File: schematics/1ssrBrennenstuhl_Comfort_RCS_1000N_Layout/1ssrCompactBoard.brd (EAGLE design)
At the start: 46 x 47 mm, 20 parts, among them K1 AQG12105

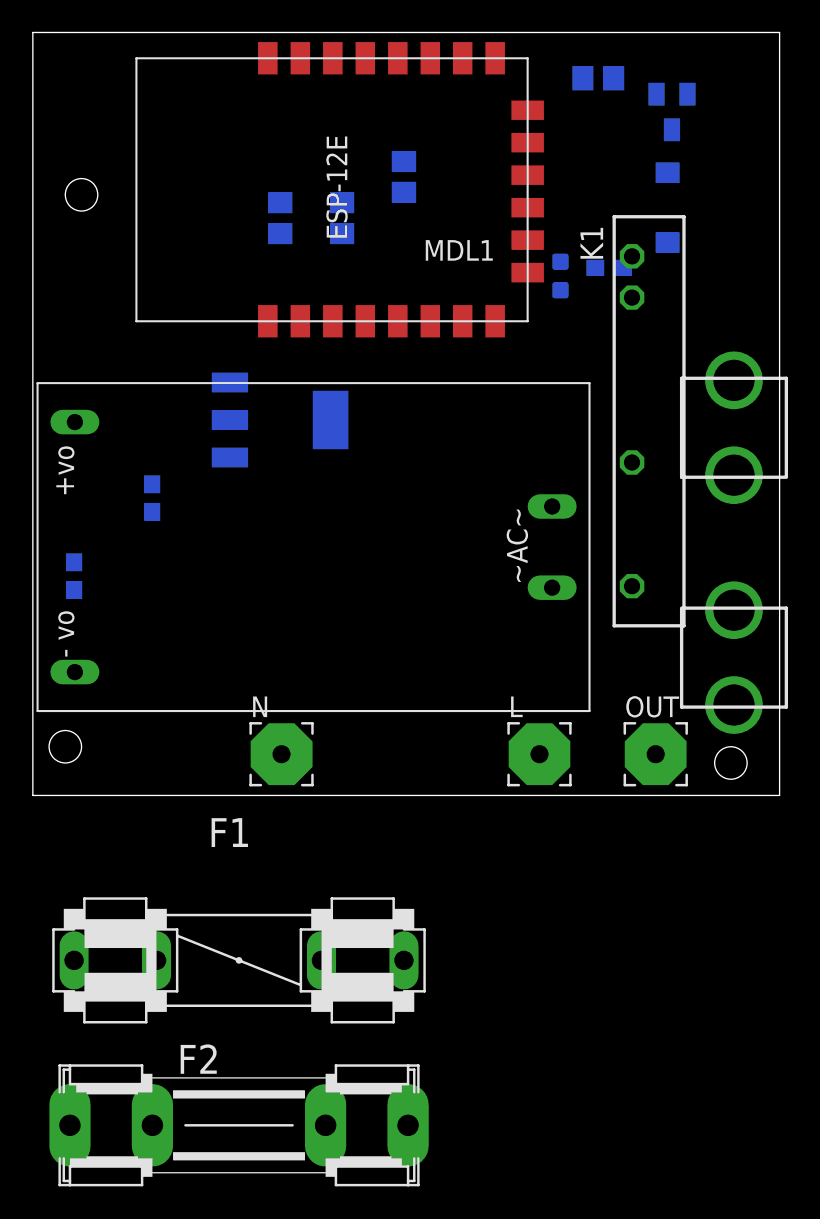
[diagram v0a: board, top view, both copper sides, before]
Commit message: placed fuse on pcb
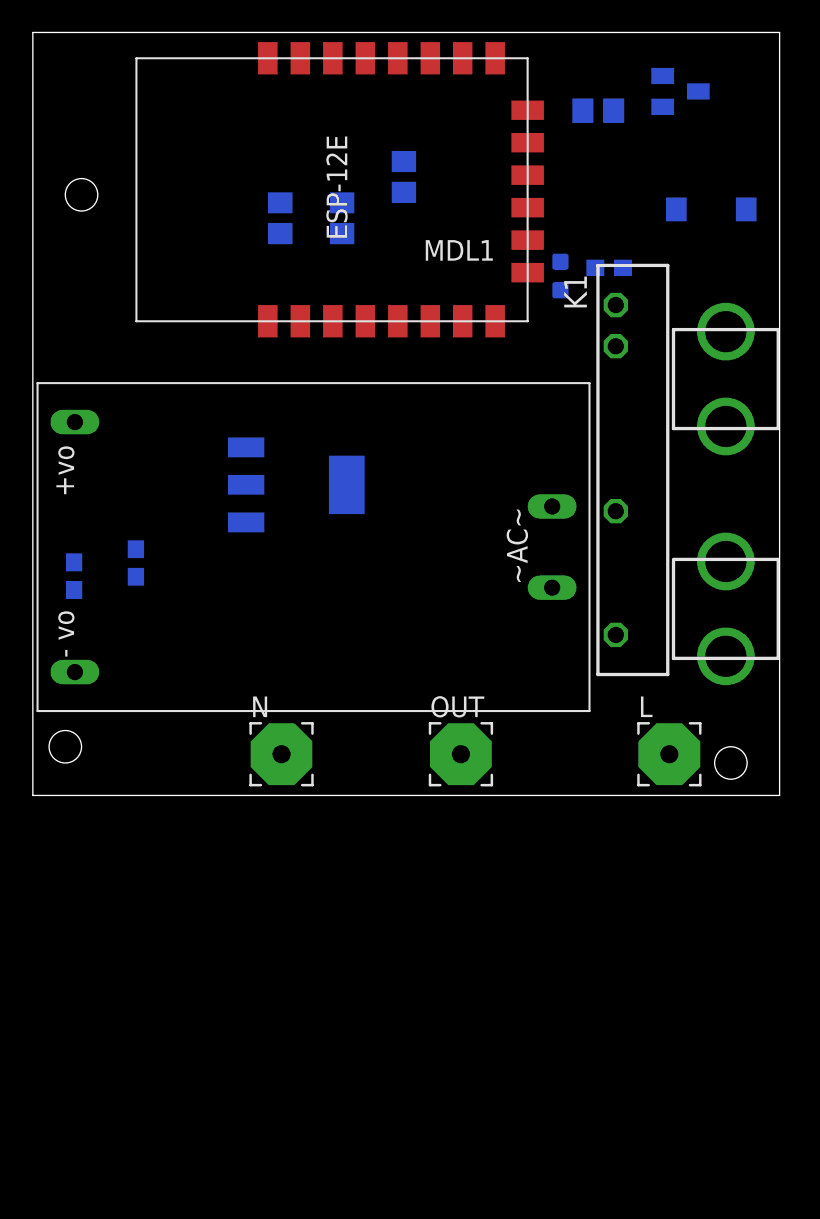
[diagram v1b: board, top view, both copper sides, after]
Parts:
- removed F1: (no value), special:FUSE1
- removed F2: (no value), fuse:SHK20L
- removed F3: FUSEX20MM, SparkFun-Passives:FUSE_5MM
- added FUSE: FUSEX20MM, SparkFun-Passives:FUSE_5MM
- moved OUT 12.0 mm to (26.4, 2.54)
- moved L 8.00 mm to (39.2, 2.54)
- moved C2 4.12 mm to (6.35, 14.3)
- moved U2 4.12 mm to (16.2, 19.1)
- moved K1 3.16 mm to (35.9, 20.1)
- moved D1 2.69 mm to (41.8, 36.1), turned to 180 degrees
- moved R3 2.00 mm to (34.8, 42.2)
- moved Q1 1.38 mm to (39.9, 43.4), turned to 90 degrees
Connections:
- net ACLOUT renamed OUT
- removed net ACLIN: K1.O1, L.1, U$4.AC1
- removed net ACN: N.1, U$4.AC2
- new net FUSED_LINE: FUSE.3, K1.O1, U$4.AC2
- new net LINE: FUSE.1, L.1
- new net NEUTRAL: N.1, U$4.AC1

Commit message: board routing work in progress
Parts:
- added J1: (no value), SparkFun-Connectors:1X02_LONGPADS
- added R6: 10K, resistor:R0805
- moved R4 5.41 mm to (32.5, 28.0), turned to 270 degrees
- moved Q1 4.81 mm to (36.6, 39.9), turned to 180 degrees
- moved D1 3.58 mm to (38.3, 35.4)
- moved R1 3.18 mm to (25.0, 35.8)
- moved OUT 2.50 mm to (28.9, 2.54)
- moved FUSE 2.00 mm to (42.7, 16.6)
- moved R5 1.90 mm to (14.5, 33.8)
- moved R2 1.83 mm to (18.5, 33.8)
- moved C1 1.75 mm to (2.54, 11.8)
- moved R3 1.42 mm to (33.4, 41.9), turned to 270 degrees
- moved C2 1.33 mm to (6.50, 13.0)
- moved MDL1 1.00 mm to (30.5, 28.2)
- moved U$4 0.50 mm to (34.3, 24.9)
- moved U2 0.27 mm to (16.0, 19.0)
- moved K1 0.25 mm to (35.9, 19.8)
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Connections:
- net 3V3: now also R6.2
- net GND: now also J1.1
- net GPIO4: now also J1.2, R6.1
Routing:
- net GND: track 0.00 -> 97.3 mm, vias 0 -> 1
- net 5V: track 0.00 -> 57.4 mm
- net 3V3: track 0.00 -> 55.8 mm, vias 0 -> 2
- net GPIO4: track 0.00 -> 28.1 mm, vias 0 -> 1
- net NEUTRAL: track 0.00 -> 19.3 mm
- net FUSED_LINE: track 0.00 -> 17.6 mm
- net GPIO5: track 0.00 -> 17.0 mm, vias 0 -> 1
- net N$10: track 0.00 -> 13.6 mm
- net LINE: track 0.00 -> 11.1 mm
- net OUT: track 0.00 -> 10.00 mm
- net GPIO0: track 0.00 -> 8.71 mm, vias 0 -> 1
- net N$9: track 0.00 -> 4.65 mm, vias 0 -> 1
- net N$6: track 0.00 -> 4.65 mm, vias 0 -> 1
- net N$1: track 0.00 -> 2.27 mm
- net N$12: track 0.00 -> 2.24 mm

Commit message: board routing work in progress
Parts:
- moved L 1.00 mm to (38.5, 2.54)
- moved U$4 0.25 mm to (34.0, 24.9)
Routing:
- net FUSED_LINE: track 17.6 -> 11.8 mm
- net LINE: track 11.1 -> 5.84 mm
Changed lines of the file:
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@@
 <element name="R3" library="resistor" package="R0805" value="10K" x="33.43" y="41.92" rot="MR270"/>
 <element name="R5" library="resistor" package="R0805" value="10K" x="14.5" y="33.81" rot="MR270"/>
-<element name="U$4" library="hlk-pm01" package="HLK-PM01" value="HLK-PM01" x="34.29" y="24.9" rot="R180"/>
+<element name="U$4" library="hlk-pm01" package="HLK-PM01" value="HLK-PM01" x="34.04" y="24.9" rot="R180"/>
 <element name="U2" library="SparkFun-PowerIC" package="SOT223" value="" x="16" y="19" rot="MR90">
 <attribute name="PROD_ID" value="VREG-08170" x="16" y="19" size="1.778" layer="28" rot="MR90" display="off"/>
@@
 <element name="R1" library="resistor" package="R0805" value="10K" x="25" y="35.75" rot="MR270"/>
 <element name="N" library="wirepad" package="3,81/1,1" value="" x="15.32" y="2.54"/>
-<element name="L" library="wirepad" package="3,81/1,1" value="" x="39.46" y="2.54"/>
+<element name="L" library="wirepad" package="3,81/1,1" value="" x="38.46" y="2.54"/>
 <element name="OUT" library="wirepad" package="3,81/1,1" value="" x="28.87" y="2.54"/>
 <element name="D2" library="SparkFun-LED" package="LED-0603" value="" x="32.5" y="32" rot="MR0"/>
@@
 <wire x1="37.5559875" y1="43.5640125" x2="34.606975" y2="46" width="0.4064" layer="16" curve="45"/>
 <wire x1="34.606975" y1="46" x2="28.5" y2="46" width="0.4064" layer="16"/>
-<wire x1="2.59" y1="7.1" x2="4.836975" y2="7.1" width="0.4064" layer="1"/>
+<wire x1="2.34" y1="7.1" x2="4.836975" y2="7.1" width="0.4064" layer="1"/>
 <wire x1="4.836975" y1="7.1" x2="5.2859875" y2="7.2859875" width="0.4064" layer="1" curve="45"/>
 <wire x1="5.2859875" y1="7.2859875" x2="6" y2="8" width="0.4064" layer="1"/>
@@
 <wire x1="6" y1="37.486975" x2="5.8140125" y2="37.9359875" width="0.4064" layer="1" curve="45"/>
 <wire x1="5.8140125" y1="37.9359875" x2="3" y2="40.75" width="0.4064" layer="1"/>
-<wire x1="2.59" y1="7.1" x2="2.59" y2="10.789290625" width="0.4064" layer="16"/>
+<wire x1="2.34" y1="7.1" x2="2.59" y2="10.789290625" width="0.4064" layer="16"/>
 <wire x1="2.59" y1="10.789290625" x2="2.54" y2="10.91" width="0.4064" layer="16" curve="45"/>
 </signal>
@@
 <contactref element="R4" pad="2"/>
 <wire x1="2.54" y1="12.61" x2="2.59" y2="12.61" width="0.4064" layer="16"/>
-<wire x1="2.59" y1="12.61" x2="2.59" y2="22.5" width="0.4064" layer="16"/>
+<wire x1="2.59" y1="12.61" x2="2.34" y2="22.5" width="0.4064" layer="16"/>
 <wire x1="32.5" y1="27.15" x2="35.376975" y2="27.15" width="0.4064" layer="16"/>
 <wire x1="35.376975" y1="27.15" x2="35.8259875" y2="27.3359875" width="0.4064" layer="16" curve="45"/>
@@
 <wire x1="38.25" y1="30.023025" x2="38.0640125" y2="29.5740125" width="0.4064" layer="16" curve="-45"/>
 <wire x1="38.0640125" y1="29.5740125" x2="35.91" y2="27.42" width="0.4064" layer="16"/>
-<wire x1="2.59" y1="22.5" x2="6.736975" y2="22.5" width="0.4064" layer="16"/>
+<wire x1="2.34" y1="22.5" x2="6.736975" y2="22.5" width="0.4064" layer="16"/>
 <wire x1="6.736975" y1="22.5" x2="7.1859875" y2="22.3140125" width="0.4064" layer="16" curve="-45"/>
 <wire x1="7.1859875" y1="22.3140125" x2="8.25" y2="21.25" width="0.4064" layer="16"/>
@@
 <contactref element="N" pad="1"/>
 <contactref element="U$4" pad="AC1"/>
-<wire x1="31.99" y1="12.3" x2="15.32" y2="2.54" width="2.54" layer="1"/>
+<wire x1="31.74" y1="12.3" x2="15.32" y2="2.54" width="2.54" layer="1"/>
 </signal>
 <signal name="LINE" class="1">
 <contactref element="L" pad="1"/>
 <contactref element="FUSE" pad="1"/>
-<wire x1="39.46" y1="2.54" x2="42.69" y2="6.57" width="3.81" layer="1"/>
-<wire x1="42.69" y1="6.57" x2="42.75" y2="12.5" width="3.81" layer="1"/>
+<wire x1="38.46" y1="2.54" x2="42.69" y2="6.57" width="3.81" layer="1"/>
+<wire x1="42.69" y1="6.57" x2="42.75" y2="12.5" width="0" layer="19" extent="1-16"/>
 <wire x1="42.75" y1="12.5" x2="42.69" y2="6.57" width="0" layer="19" extent="1-16"/>
 </signal>
@@
 <contactref element="OUT" pad="1"/>
 <contactref element="K1" pad="O2"/>
-<wire x1="28.87" y1="2.54" x2="35.91" y2="9.64" width="2.54" layer="16"/>
+<wire x1="28.87" y1="2.54" x2="34.75" y2="8" width="2.54" layer="16"/>
+<wire x1="34.75" y1="8" x2="35.91" y2="9.64" width="2.05" layer="16"/>
 </signal>
 <signal name="FUSED_LINE" class="1">
@@
 <contactref element="K1" pad="O1"/>
 <contactref element="FUSE" pad="3"/>
-<wire x1="42.69" y1="20.728" x2="35.91" y2="17.26" width="3.81" layer="1"/>
-<wire x1="35.91" y1="17.26" x2="31.99" y2="17.3" width="1.778" layer="1"/>
-<wire x1="42.69" y1="20.728" x2="42.69" y2="26.605146875" width="3.81" layer="1"/>
-<wire x1="42.69" y1="26.605146875" x2="42.75" y2="26.75" width="0.4064" layer="1" curve="-45"/>
-<wire x1="42.75" y1="26.75" x2="42.69" y2="20.728" width="0" layer="19" extent="1-16"/>
+<wire x1="35.91" y1="17.26" x2="31.74" y2="17.3" width="1.778" layer="1"/>
+<wire x1="35.91" y1="17.26" x2="42.69" y2="20.728" width="3.81" layer="1"/>
 </signal>
 <signal name="GPIO4">
